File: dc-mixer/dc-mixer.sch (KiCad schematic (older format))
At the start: 20 parts, among them J1 Conn_01x01_Female, J2 Conn_01x01_Female, J3 Conn_01x01_Female, J4 Conn_01x01_Female, J5 Conn_01x01_Female, J6 Conn_01x01_Female, J7 Conn_01x01_Female, J8 Conn_01x04_Male, J9 Conn_01x01_Female, U1 TL072

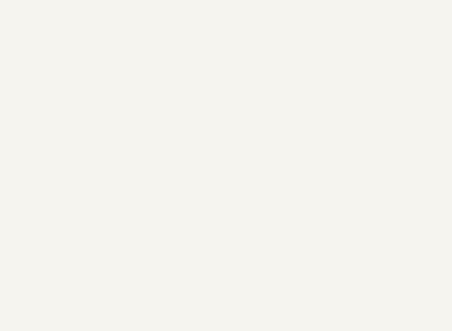
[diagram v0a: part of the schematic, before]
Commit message: Adding screws to mixer schematic
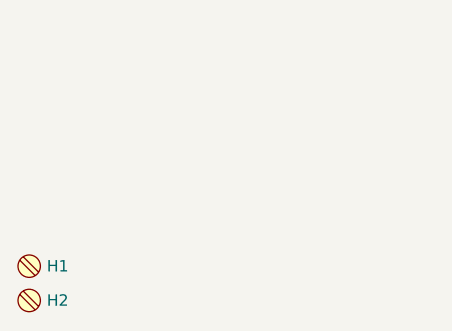
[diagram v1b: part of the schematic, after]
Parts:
- added H1, H2: MountingScrew_M3_Flathead, MountingHole:MountingHole_3.2mm_M3, symbol Board_Hardware:MountingScrew_M3_Flathead
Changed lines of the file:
@@
 Wire Wire Line
 	9100 4550 9600 4550
+$Comp
+L Board_Hardware:MountingScrew_M3_Flathead H1
+U 1 1 6030CCDB
+P 1450 6300
+F 0 "H1" H 1527 6300 50  0000 L CNN
+F 1 "MountingScrew_M3_Flathead" H 1450 6200 50  0001 C CNN
+F 2 "MountingHole:MountingHole_3.2mm_M3" H 1450 6100 50  0001 C CNN
+F 3 "" H 1450 6300 50  0001 C CNN
+	1    1450 6300
+	1    0    0    -1
+$EndComp
+$Comp
+L Board_Hardware:MountingScrew_M3_Flathead H2
+U 1 1 6030CFC1
+P 1450 6450
+F 0 "H2" H 1527 6450 50  0000 L CNN
+F 1 "MountingScrew_M3_Flathead" H 1450 6350 50  0001 C CNN
+F 2 "MountingHole:MountingHole_3.2mm_M3" H 1450 6250 50  0001 C CNN
+F 3 "" H 1450 6450 50  0001 C CNN
+	1    1450 6450
+	1    0    0    -1
+$EndComp
 $EndSCHEMATC

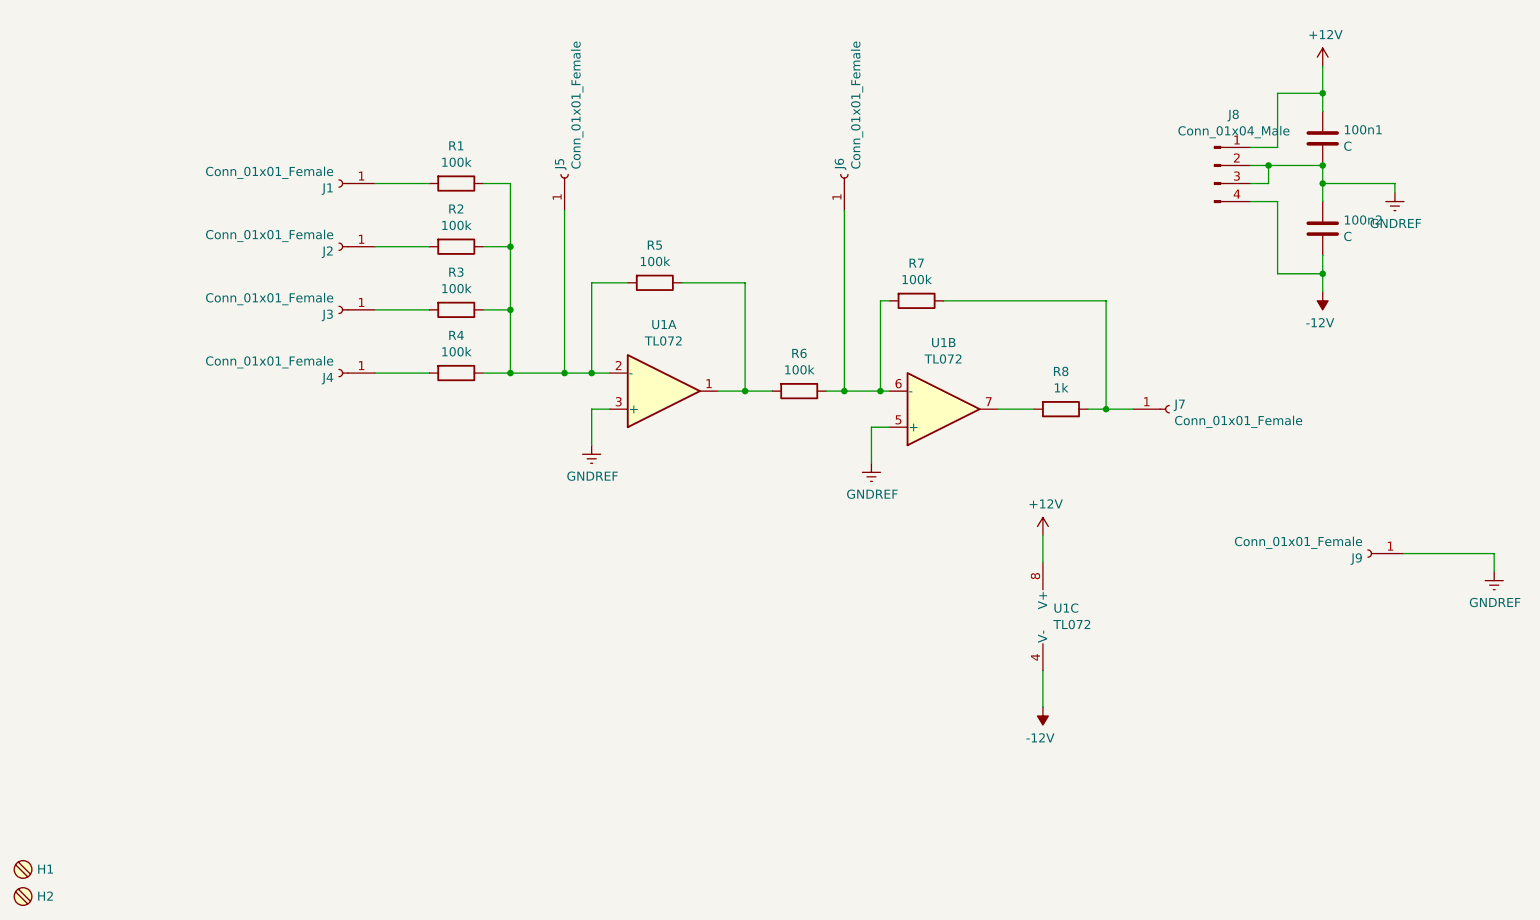
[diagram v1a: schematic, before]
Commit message: adding opamp feedback caps to dc mixer
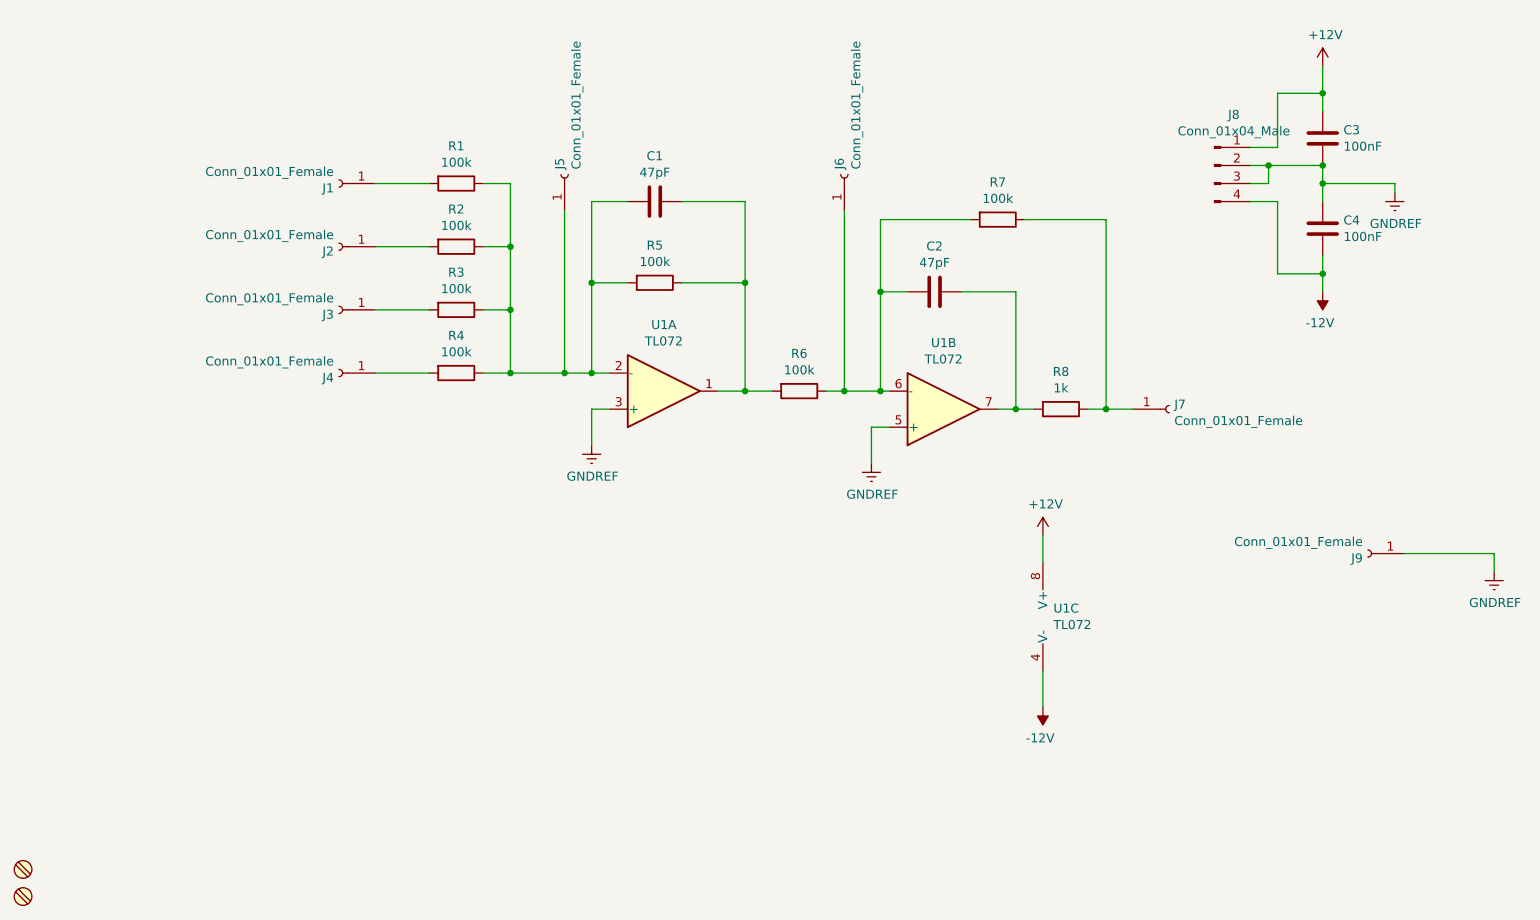
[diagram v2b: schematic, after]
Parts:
- removed 100n1, 100n2: C, Capacitor_THT:C_Rect_L7.0mm_W3.5mm_P5.00mm, symbol Device:C
- added C1, C2: 47pF, Capacitor_THT:C_Rect_L7.0mm_W3.5mm_P5.00mm, symbol Device:C
- added C3, C4: 100nF, Capacitor_THT:C_Rect_L7.0mm_W3.5mm_P5.00mm, symbol Device:C
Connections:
- net +12V: now also C3.1
- net -12V: now also C4.2
- net GNDREF: now also C3.2, C4.1
- net at R5.1, R6.2, U1.1: now also C1.1
- net at J5.1 (Pin_1), R1.1, R2.1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: now also C1.2
- net at J6.1 (Pin_1), R6.1, R7.2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: now also C2.2
- net at R8.2, U1.7: now also C2.1
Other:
- moved on the sheet: R7
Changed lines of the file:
@@
-$EndComp
-$Comp
-L Device:R R7
-U 1 1 600D8EAF
-P 6400 3150
-F 0 "R7" V 6193 3150 50  0000 C CNN
-F 1 "100k" V 6284 3150 50  0000 C CNN
-F 2 "Resistor_THT:R_Axial_DIN0207_L6.3mm_D2.5mm_P10.16mm_Horizontal" V 6330 3150 50  0001 C CNN
-F 3 "~" H 6400 3150 50  0001 C CNN
-	1    6400 3150
-	0    1    1    0
 $EndComp
 $Comp
@@
 Connection ~ 6000 3650
 Wire Wire Line
-	6250 3150 6200 3150
-Wire Wire Line
-	6200 3150 6200 3650
-Wire Wire Line
 	6000 3650 6200 3650
 Connection ~ 6200 3650
@@
 	6200 3650 6250 3650
 Wire Wire Line
-	6850 3750 7050 3750
+	6850 3750 6950 3750
 Wire Wire Line
 	7100 4450 7100 4600
@@
 $EndComp
 Wire Wire Line
-	6550 3150 7450 3150
-Wire Wire Line
-	7450 3150 7450 3750
-Wire Wire Line
 	8250 2400 8350 2400
 Wire Wire Line
@@
 Wire Wire Line
 	8350 2400 8650 2400
-Connection ~ 8650 2400
 Wire Wire Line
 	8650 2900 8650 3000
@@
 $EndComp
 $Comp
-L Device:C 100n2
-U 1 1 600DB516
-P 8650 2750
-F 0 "100n2" H 8765 2796 50  0000 L CNN
-F 1 "C" H 8765 2705 50  0000 L CNN
-F 2 "Capacitor_THT:C_Rect_L7.0mm_W3.5mm_P5.00mm" H 8688 2600 50  0001 C CNN
-F 3 "~" H 8650 2750 50  0001 C CNN
-	1    8650 2750
-	1    0    0    -1
-$EndComp
-$Comp
-L Device:C 100n1
-U 1 1 600DAE96
-P 8650 2250
-F 0 "100n1" H 8765 2296 50  0000 L CNN
-F 1 "C" H 8765 2205 50  0000 L CNN
-F 2 "Capacitor_THT:C_Rect_L7.0mm_W3.5mm_P5.00mm" H 8688 2100 50  0001 C CNN
-F 3 "~" H 8650 2250 50  0001 C CNN
-	1    8650 2250
-	1    0    0    -1
-$EndComp
-$Comp
 L Connector:Conn_01x01_Female J9
 U 1 1 601C1072
@@
 U 1 1 6030CCDB
 P 1450 6300
-F 0 "H1" H 1527 6300 50  0000 L CNN
+F 0 "H1" H 1527 6300 50  0001 L CNN
 F 1 "MountingScrew_M3_Flathead" H 1450 6200 50  0001 C CNN
 F 2 "MountingHole:MountingHole_3.2mm_M3" H 1450 6100 50  0001 C CNN
@@
 U 1 1 6030CFC1
 P 1450 6450
-F 0 "H2" H 1527 6450 50  0000 L CNN
+F 0 "H2" H 1527 6450 50  0001 L CNN
 F 1 "MountingScrew_M3_Flathead" H 1450 6350 50  0001 C CNN
 F 2 "MountingHole:MountingHole_3.2mm_M3" H 1450 6250 50  0001 C CNN
@@
 	1    0    0    -1
 $EndComp
+$Comp
+L Device:C C1
+U 1 1 60E36C29
+P 4950 2600
+F 0 "C1" V 4698 2600 50  0000 C CNN
+F 1 "47pF" V 4789 2600 50  0000 C CNN
+F 2 "Capacitor_THT:C_Rect_L7.0mm_W3.5mm_P5.00mm" H 4988 2450 50  0001 C CNN
+F 3 "~" H 4950 2600 50  0001 C CNN
+	1    4950 2600
+	0    1    1    0
+$EndComp
+$Comp
+L Device:C C2
+U 1 1 60E3A0A1
+P 6500 3100
+F 0 "C2" V 6248 3100 50  0000 C CNN
+F 1 "47pF" V 6339 3100 50  0000 C CNN
+F 2 "Capacitor_THT:C_Rect_L7.0mm_W3.5mm_P5.00mm" H 6538 2950 50  0001 C CNN
+F 3 "~" H 6500 3100 50  0001 C CNN
+	1    6500 3100
+	0    1    1    0
+$EndComp
+Wire Wire Line
+	4600 3050 4600 2600
+Wire Wire Line
+	4600 2600 4800 2600
+Connection ~ 4600 3050
+Wire Wire Line
+	5100 2600 5450 2600
+Wire Wire Line
+	5450 2600 5450 3050
+Connection ~ 5450 3050
+Wire Wire Line
+	6350 3100 6200 3100
+Connection ~ 6200 3100
+Wire Wire Line
+	6200 3100 6200 3650
+Wire Wire Line
+	6650 3100 6950 3100
+Wire Wire Line
+	6950 3100 6950 3750
+Connection ~ 6950 3750
+Wire Wire Line
+	6950 3750 7050 3750
+$Comp
+L Device:R R7
+U 1 1 600D8EAF
+P 6850 2700
+F 0 "R7" V 6643 2700 50  0000 C CNN
+F 1 "100k" V 6734 2700 50  0000 C CNN
+F 2 "Resistor_THT:R_Axial_DIN0207_L6.3mm_D2.5mm_P10.16mm_Horizontal" V 6780 2700 50  0001 C CNN
+F 3 "~" H 6850 2700 50  0001 C CNN
+	1    6850 2700
+	0    1    1    0
+$EndComp
+Wire Wire Line
+	6200 2700 6700 2700
+Wire Wire Line
+	7000 2700 7450 2700
+Wire Wire Line
+	6200 2700 6200 3100
+Wire Wire Line
+	7450 2700 7450 3750
+$Comp
+L Device:C C3
+U 1 1 60E8538F
+P 8650 2250
+F 0 "C3" H 8765 2296 50  0000 L CNN
+F 1 "100nF" H 8765 2205 50  0000 L CNN
+F 2 "Capacitor_THT:C_Rect_L7.0mm_W3.5mm_P5.00mm" H 8688 2100 50  0001 C CNN
+F 3 "~" H 8650 2250 50  0001 C CNN
+	1    8650 2250
+	1    0    0    -1
+$EndComp
+Connection ~ 8650 2400
+$Comp
+L Device:C C4
+U 1 1 60E85957
+P 8650 2750
+F 0 "C4" H 8765 2796 50  0000 L CNN
+F 1 "100nF" H 8765 2705 50  0000 L CNN
+F 2 "Capacitor_THT:C_Rect_L7.0mm_W3.5mm_P5.00mm" H 8688 2600 50  0001 C CNN
+F 3 "~" H 8650 2750 50  0001 C CNN
+	1    8650 2750
+	1    0    0    -1
+$EndComp
